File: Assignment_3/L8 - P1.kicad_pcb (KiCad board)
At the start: 2 copper layers, 21 parts, among them J1 Screw_Terminal_01x02, J2 Screw_Terminal_01x02, J3 Screw_Terminal_01x03, J4 Conn_01x04_Pin, J5 Conn_01x02_Pin, J6 Conn_01x02_Pin, J7 Conn_01x02_Pin, U1 L298N, U2 LM7805_TO220

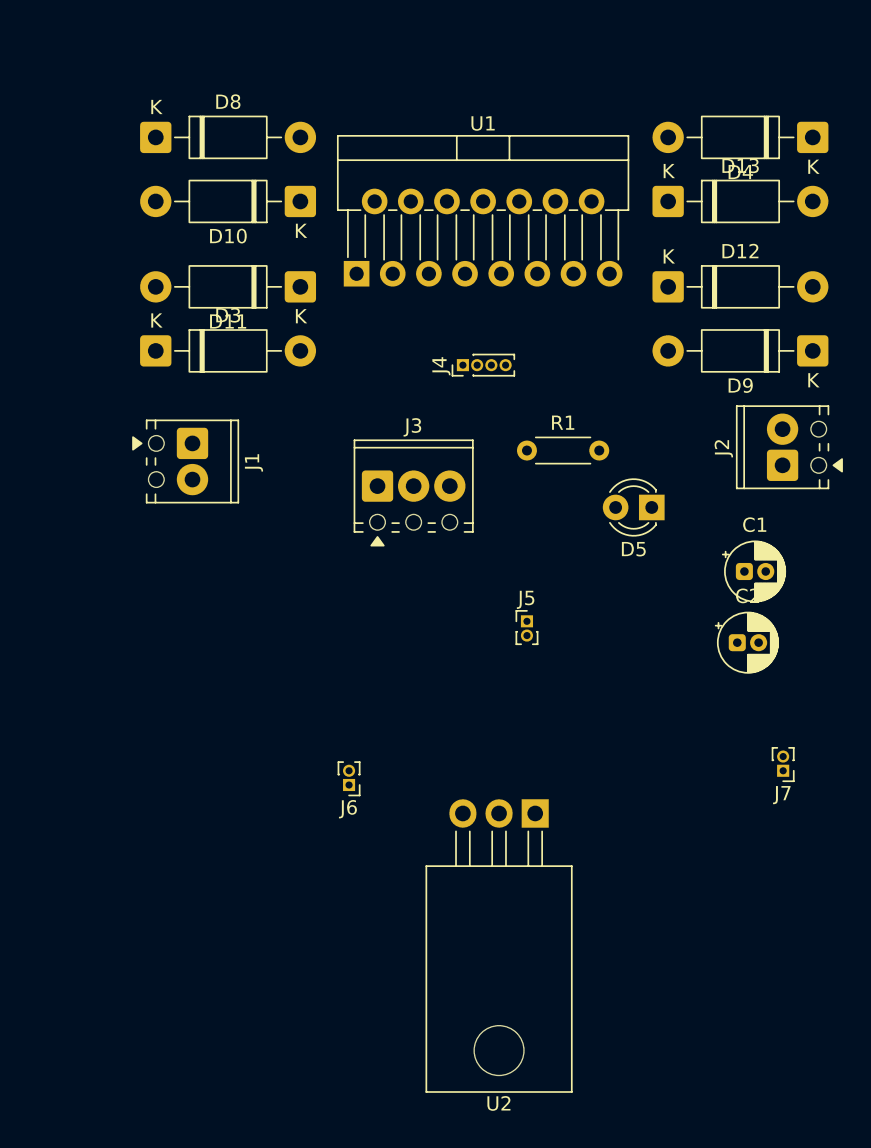
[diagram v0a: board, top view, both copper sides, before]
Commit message: Update layout of all assignments
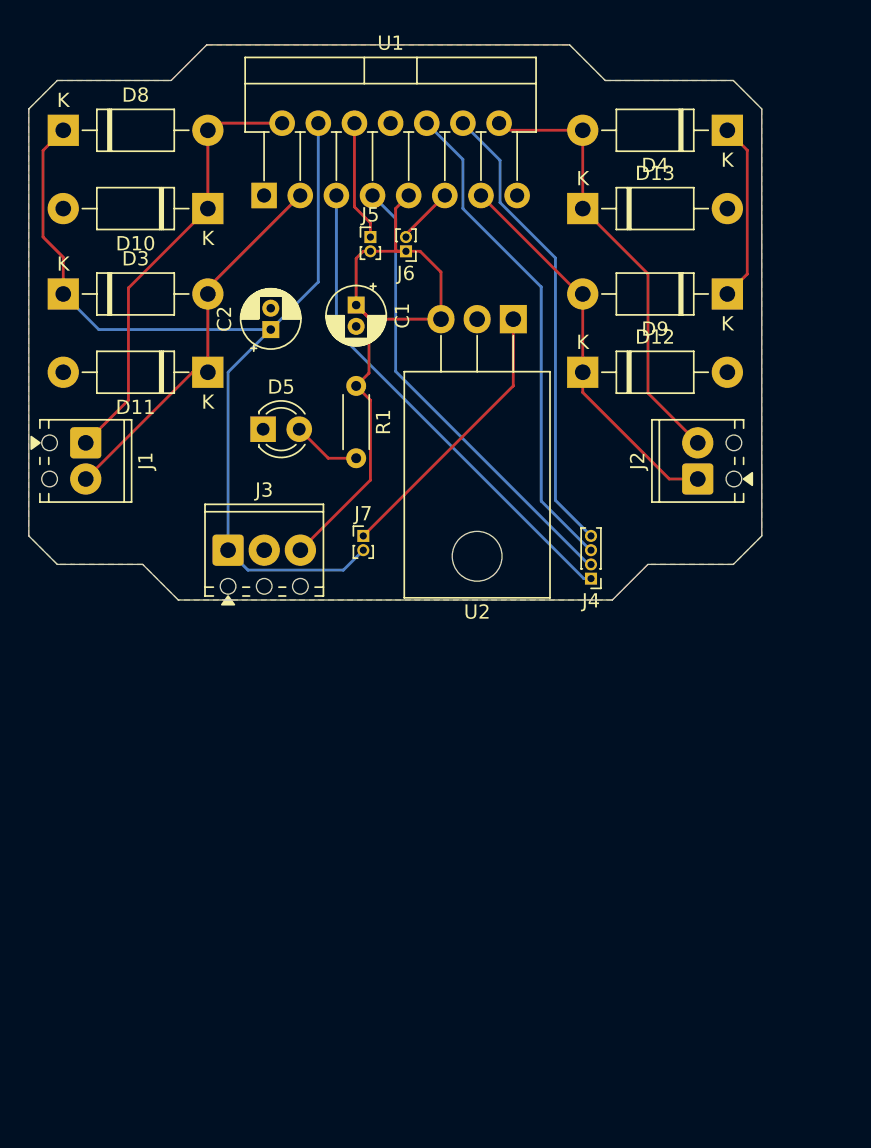
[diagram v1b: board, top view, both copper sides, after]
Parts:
- moved C2 39.5 mm to (142.5, 65.5), turned to 90 degrees
- moved J6 37.7 mm to (152.0, 60.0)
- moved U2 34.8 mm to (159.5, 64.8)
- moved J7 33.8 mm to (149.0, 80.0), turned to 0 degrees
- moved C1 33.1 mm to (148.5, 63.8), turned to -90 degrees
- moved J5 29.2 mm to (149.5, 59.0)
- moved D5 27.9 mm to (142.0, 72.5), turned to 0 degrees
- moved J4 17.5 mm to (165.0, 83.0), turned to 180 degrees
- moved R1 12.8 mm to (148.5, 69.5), turned to -90 degrees
- moved J3 11.4 mm to (139.5, 81.0)
- moved D11 8.85 mm to (138.1, 68.5)
- moved U1 8.51 mm to (142.0, 56.1)
- moved D12 8.49 mm to (164.4, 68.5)
- moved D3 7.63 mm to (127.9, 63.0)
- moved J1 7.50 mm to (129.5, 73.5)
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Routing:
- net /7-35V: track 0.00 -> 84.2 mm
- net /5V: track 0.00 -> 45.1 mm
- net Net-(J4-Pin_3): track 0.00 -> 34.8 mm
- net Net-(J4-Pin_1): track 0.00 -> 34.6 mm
- net Net-(J4-Pin_4): track 0.00 -> 32.7 mm
- net Net-(J4-Pin_2): track 0.00 -> 32.4 mm
- net Net-(D13-K): track 0.00 -> 31.4 mm
- net Net-(D10-K): track 0.00 -> 30.9 mm
- net Net-(D12-K): track 0.00 -> 27.5 mm
- net Net-(D11-K): track 0.00 -> 26.8 mm
- net Net-(J7-Pin_1): track 0.00 -> 19.6 mm
- net Net-(J5-Pin_1): track 0.00 -> 8.46 mm
- net Net-(D5-A): track 0.00 -> 4.84 mm
- net Net-(J6-Pin_2): track 0.00 -> 4.05 mm
- added copper zone on F.Cu, net GND
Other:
- board outline added: 51.5 x 39 mm

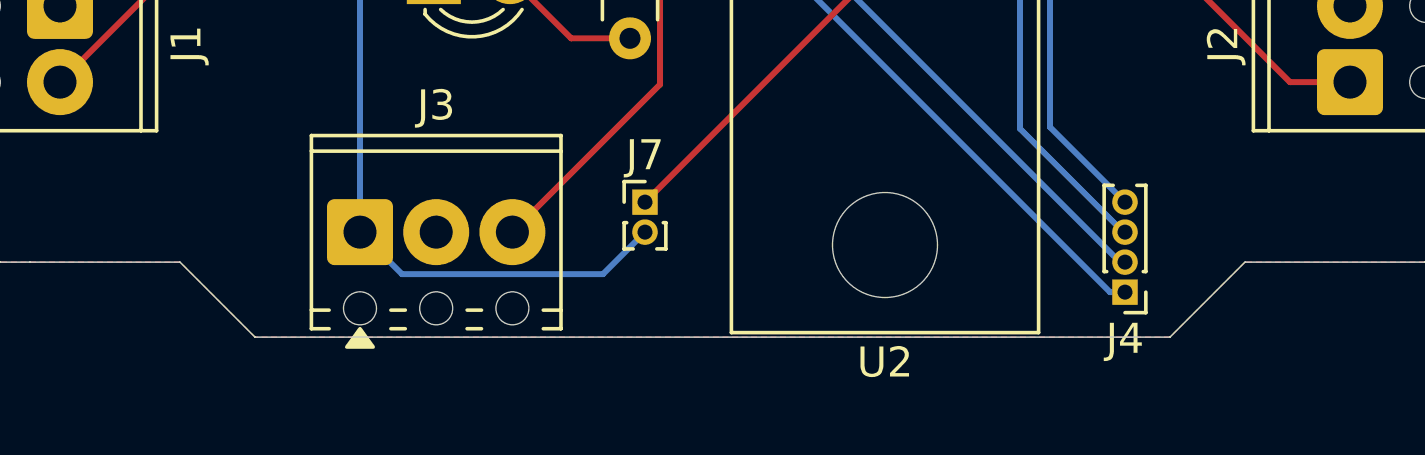
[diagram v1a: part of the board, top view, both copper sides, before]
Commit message: Update layout of all assignments - P2
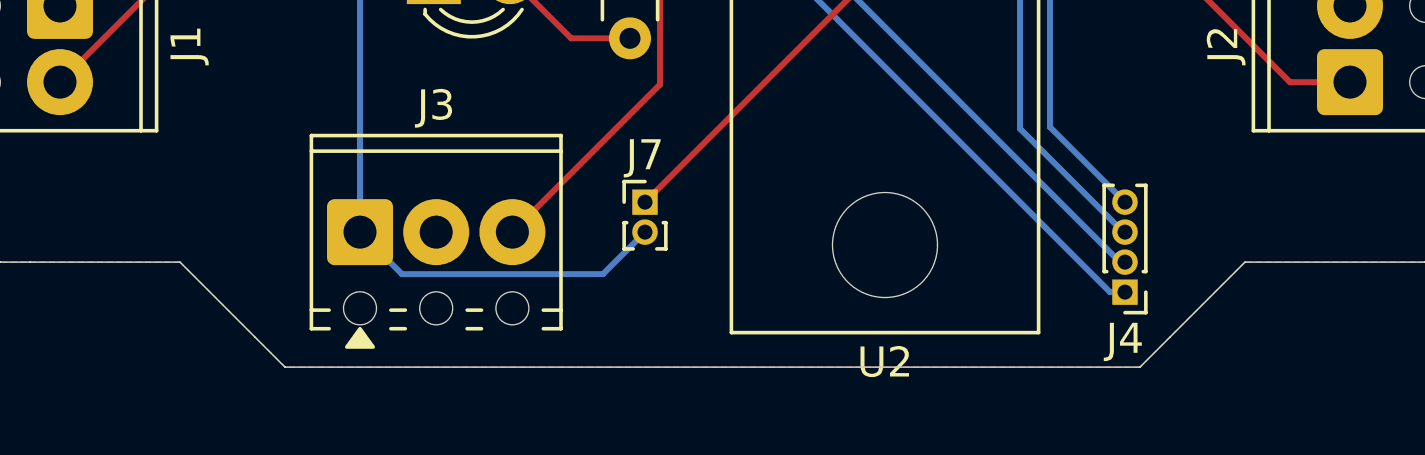
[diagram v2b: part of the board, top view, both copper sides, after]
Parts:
- added G***: LOGO, Logo:logo, B.Cu at (136.0, 75.0)
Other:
- board size 51.5 x 39 mm -> 51.5 x 40 mm
- board text added: "Name: Ahmed Atef Nasr ID: 1471804251201"
